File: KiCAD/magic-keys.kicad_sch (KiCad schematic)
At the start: 157 parts, among them J1 Keyswitch, K1 Keyswitch, M1 Keyswitch, P1 Keyswitch, Q1 Keyswitch, T1 Keyswitch, U1 Raspberry_Pi_Pico, U2 Keyswitch, X1 Keyswitch, Y1 Keyswitch

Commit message: added more stuff for magickeys
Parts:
- '"1, -_1, /1, 0)1, 1!1, 2@1, 3#1, 4$1, 5%1, 6^1, 7&1, 8*1, 9(1, ;:1, <,1, =+1, >.1, A1, B1, C1, D1, Down1, E1, F1, F10, F11, F12, F13, F2, F3, F4, F5, F6, F7, F8, F9, G1, H1, I1, J1, K1, L1, Left1, M1, N1, O1, P1, Q1, R1, Right1, S1, T1, U2, Up1, V1, W1, X1, Y1, Z1, [{1, ]}1, `~1: footprint ScottoKeebs_Choc:Choc_V1_1.00u -> ScottoKeebs_Hotswap:Hotswap_Choc_V1V2_1.00u
- Backspace1: footprint ScottoKeebs_Choc:Choc_V1_2.00u -> ScottoKeebs_Hotswap:Hotswap_Choc_V1V2_2.00u
- CapsLock1: footprint ScottoKeebs_Choc:Choc_V1_1.75u -> ScottoKeebs_Hotswap:Hotswap_Choc_V1V2_1.75u
- Cmd1, Cmd2, Control1, Fn1, Option1, Option2: footprint ScottoKeebs_Choc:Choc_V1_1.25u -> ScottoKeebs_Hotswap:Hotswap_Choc_V1V2_1.00u
- Del1, Esc1, \|1: footprint ScottoKeebs_Choc:Choc_V1_1.00u -> ScottoKeebs_Hotswap:Hotswap_Choc_V1V2_1.50u
- Enter1: footprint ScottoKeebs_Choc:Choc_V1_2.00u -> ScottoKeebs_Hotswap:Hotswap_Choc_V1V2_2.25u
- Shift1: footprint ScottoKeebs_Choc:Choc_V1_2.25u -> ScottoKeebs_Hotswap:Hotswap_Choc_V1V2_2.75u
- Shift2: footprint ScottoKeebs_Choc:Choc_V1_2.75u -> ScottoKeebs_Hotswap:Hotswap_Choc_V1V2_2.25u
- Space1: footprint ScottoKeebs_Choc:Choc_V1_6.25u -> ScottoKeebs_Hotswap:Hotswap_Choc_V1V2_5.50u
- Tab1: footprint ScottoKeebs_Choc:Choc_V1_1.50u -> ScottoKeebs_Hotswap:Hotswap_Choc_V1V2_1.50u

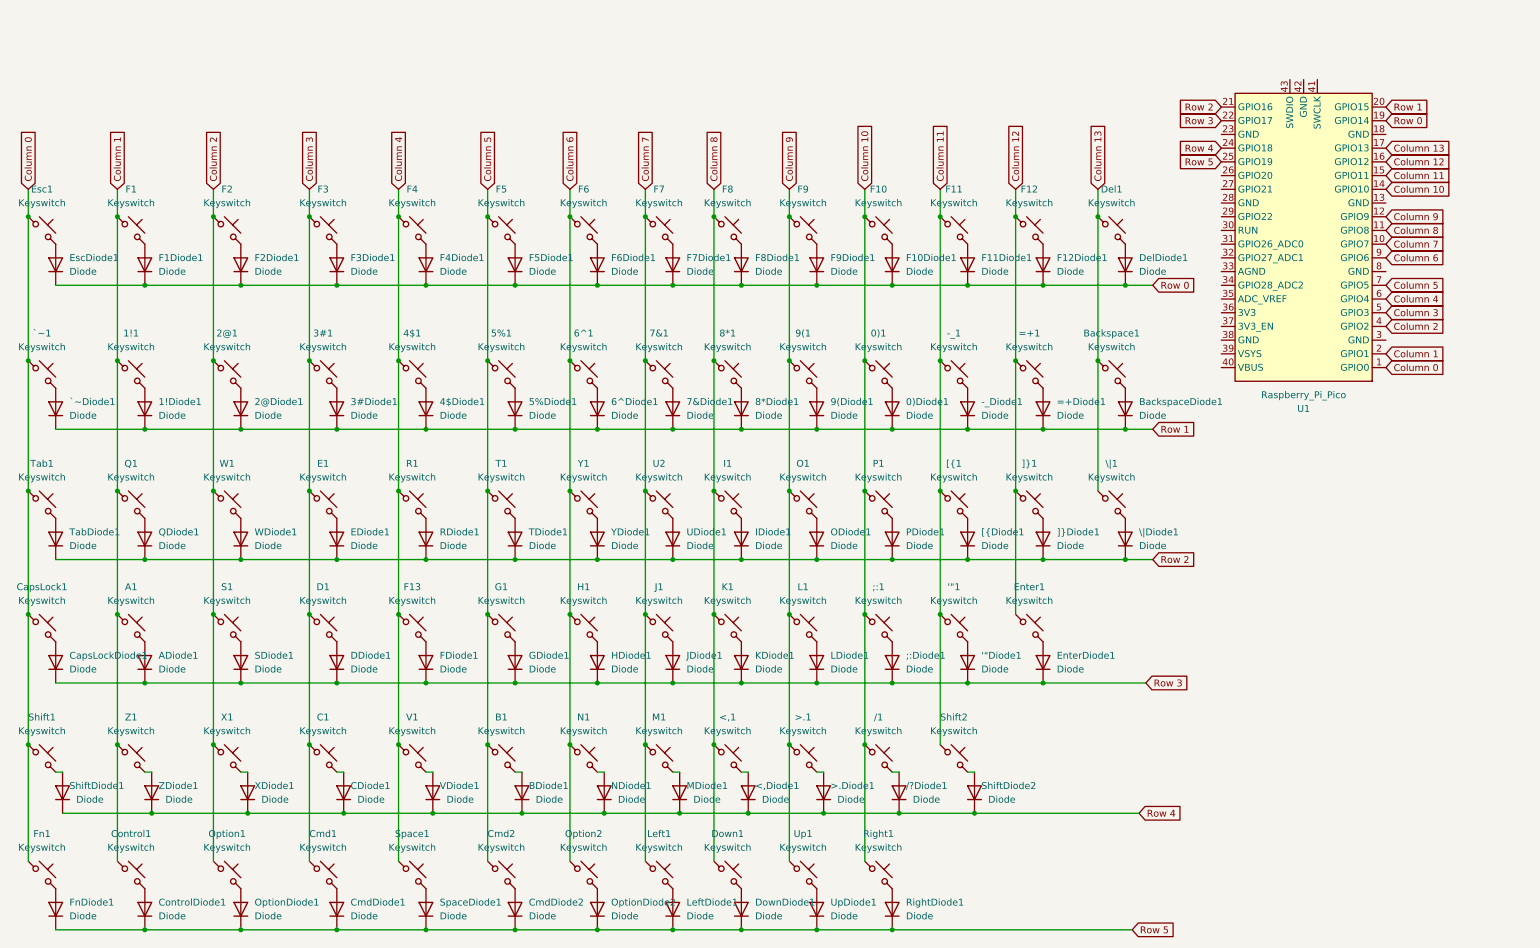
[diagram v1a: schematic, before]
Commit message: changed layout for stabs (to be keys), finished schematics
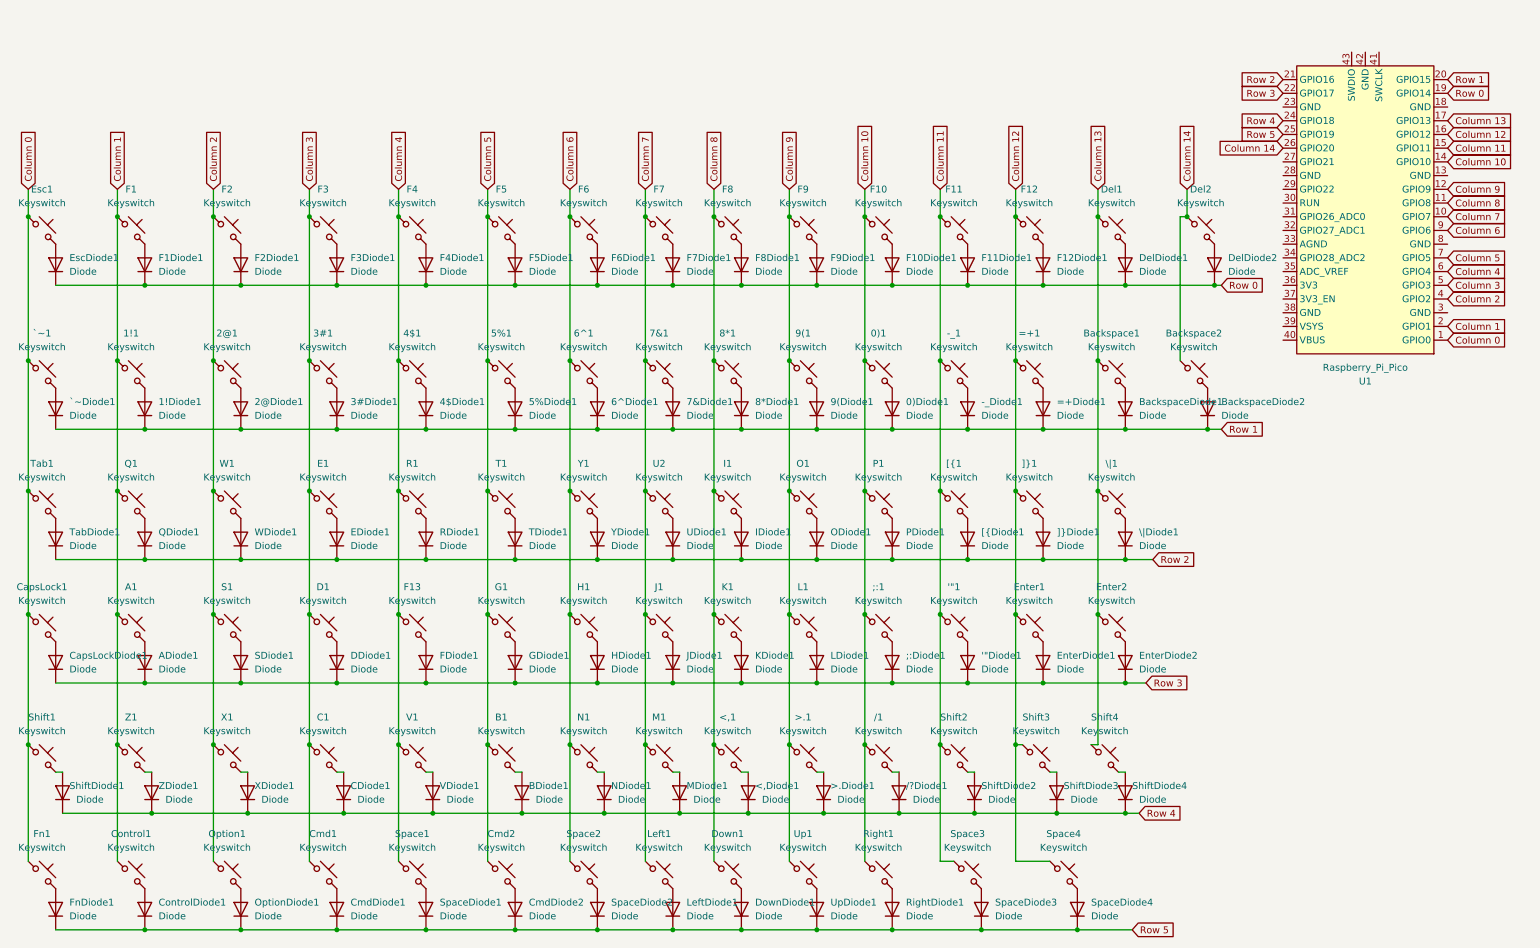
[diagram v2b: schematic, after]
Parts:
- removed Option2: Keyswitch, ScottoKeebs_Hotswap:Hotswap_Choc_V1V2_1.00u, symbol SCOTTO_KICAD_SYMBOLS:Placeholder_Keyswitch
- removed OptionDiode2: Diode, ScottoKeebs_Components:Diode_DO-35, symbol SCOTTO_KICAD_SYMBOLS:Placeholder_Diode
- added Backspace2, Del2, Shift4: Keyswitch, ScottoKeebs_Hotswap:Hotswap_Choc_V1_1.00u, symbol SCOTTO_KICAD_SYMBOLS:Placeholder_Keyswitch
- added BackspaceDiode2, DelDiode2, EnterDiode2, ShiftDiode3, ShiftDiode4, SpaceDiode2, SpaceDiode3, SpaceDiode4: Diode, ScottoKeebs_Components:Diode_DO-35, symbol SCOTTO_KICAD_SYMBOLS:Placeholder_Diode
- added Enter2: Keyswitch, ScottoKeebs_Hotswap:Hotswap_Choc_V1_1.25u, symbol SCOTTO_KICAD_SYMBOLS:Placeholder_Keyswitch
- added Shift3, Space2, Space3, Space4: Keyswitch, ScottoKeebs_Hotswap:Hotswap_Choc_V1_1.50u, symbol SCOTTO_KICAD_SYMBOLS:Placeholder_Keyswitch
- '"1, -_1, /1, 0)1, 1!1, 2@1, 3#1, 4$1, 5%1, 6^1, 7&1, 8*1, 9(1, ;:1, <,1, =+1, >.1, A1, B1, C1, Cmd1, Cmd2, Control1, D1, Down1, E1, F1, F10, F11, F12, F13, F2, F3, F4, F5, F6, F7, F8, F9, Fn1, G1, H1, I1, J1, K1, L1, Left1, M1, N1, O1, Option1, P1, Q1, R1, Right1, S1, T1, U2, Up1, V1, W1, X1, Y1, Z1, [{1, ]}1, `~1: footprint ScottoKeebs_Hotswap:Hotswap_Choc_V1V2_1.00u -> ScottoKeebs_Hotswap:Hotswap_Choc_V1_1.00u
- Backspace1: footprint ScottoKeebs_Hotswap:Hotswap_Choc_V1V2_2.00u -> ScottoKeebs_Hotswap:Hotswap_Choc_V1_1.00u
- CapsLock1: footprint ScottoKeebs_Hotswap:Hotswap_Choc_V1V2_1.75u -> ScottoKeebs_Hotswap:Hotswap_Choc_V1_1.75u
- Del1, Esc1: footprint ScottoKeebs_Hotswap:Hotswap_Choc_V1V2_1.50u -> ScottoKeebs_Hotswap:Hotswap_Choc_V1_1.00u
- Enter1: footprint ScottoKeebs_Hotswap:Hotswap_Choc_V1V2_2.25u -> ScottoKeebs_Hotswap:Hotswap_Choc_V1_1.00u
- Shift1: footprint ScottoKeebs_Hotswap:Hotswap_Choc_V1V2_2.75u -> ScottoKeebs_Hotswap:Hotswap_Choc_V1_1.25u
- Shift2: footprint ScottoKeebs_Hotswap:Hotswap_Choc_V1V2_2.25u -> ScottoKeebs_Hotswap:Hotswap_Choc_V1_1.25u
- Space1: footprint ScottoKeebs_Hotswap:Hotswap_Choc_V1V2_5.50u -> ScottoKeebs_Hotswap:Hotswap_Choc_V1_1.50u
- Tab1, \|1: footprint ScottoKeebs_Hotswap:Hotswap_Choc_V1V2_1.50u -> ScottoKeebs_Hotswap:Hotswap_Choc_V1_1.50u
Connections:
- net Column 11: now also Space3.1
- net Column 12: now also Shift3.1, Space4.1
- net Column 13: now also Enter2.1, Shift4.1
- net Column 6: now also Space2.1
- net Row 0: now also DelDiode2.1 (K)
- net Row 1: now also BackspaceDiode2.1 (K)
- net Row 3: now also EnterDiode2.1 (K)
- net Row 4: now also ShiftDiode3.1 (K), ShiftDiode4.1 (K)
- net Row 5: now also SpaceDiode2.1 (K), SpaceDiode3.1 (K), SpaceDiode4.1 (K)
- net Column 14: now reaches U1.26 (GPIO20)
- net Column 14: now also Backspace2.1, Del2.1
- new net: Backspace2.2, BackspaceDiode2.2 (A)
- new net: Shift4.2, ShiftDiode4.2 (A)
- new net: Shift3.2, ShiftDiode3.2 (A)
- new net: Space4.2, SpaceDiode4.2 (A)
- new net: Enter2.2, EnterDiode2.2 (A)
- new net: Space2.2, SpaceDiode2.2 (A)
- new net: Del2.2, DelDiode2.2 (A)
- new net: Space3.2, SpaceDiode3.2 (A)
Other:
- moved on the sheet: U1

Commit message: Optimised wiring
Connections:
- net Column 1: now also Shift3.1; no longer Z1.1
- net Column 10: now also >.1.1, Down1.1; no longer /1.1, Right1.1
- net Column 11: now also /1.1, Up1.1; no longer Shift2.1, Space3.1
- net Column 12: now also Right1.1, Shift2.1; no longer Shift3.1, Space4.1
- net Column 14: now also U1.19 (GPIO14); no longer U1.26 (GPIO20)
- net Column 2: now also Z1.1; no longer X1.1
- net Column 3: now also X1.1; no longer C1.1
- net Column 4: now also C1.1; no longer V1.1
- net Column 5: now also Space2.1, V1.1; no longer B1.1, Cmd2.1
- net Column 6: now also B1.1, Space3.1; no longer N1.1, Space2.1
- net Column 7: now also N1.1, Space4.1; no longer Left1.1, M1.1
- net Column 8: now also Cmd2.1, M1.1; no longer <,1.1, Down1.1
- net Column 9: now also <,1.1, Left1.1; no longer >.1.1, Up1.1
- net Row 0: now also U1.21 (GPIO16); no longer U1.19 (GPIO14)
- net Row 1: now also U1.22 (GPIO17); no longer U1.20 (GPIO15)
- net Row 2: now also U1.24 (GPIO18); no longer U1.21 (GPIO16)
- net Row 3: now also U1.25 (GPIO19); no longer U1.22 (GPIO17)
- net Row 4: now also U1.26 (GPIO20); no longer U1.24 (GPIO18)
- net Row 5: now also U1.27 (GPIO21); no longer U1.25 (GPIO19)
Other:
- moved on the sheet: /1, /?Diode1, <,1, <,Diode1, >.1, >.Diode1, B1, BDiode1, C1, CDiode1, Cmd2, Down1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

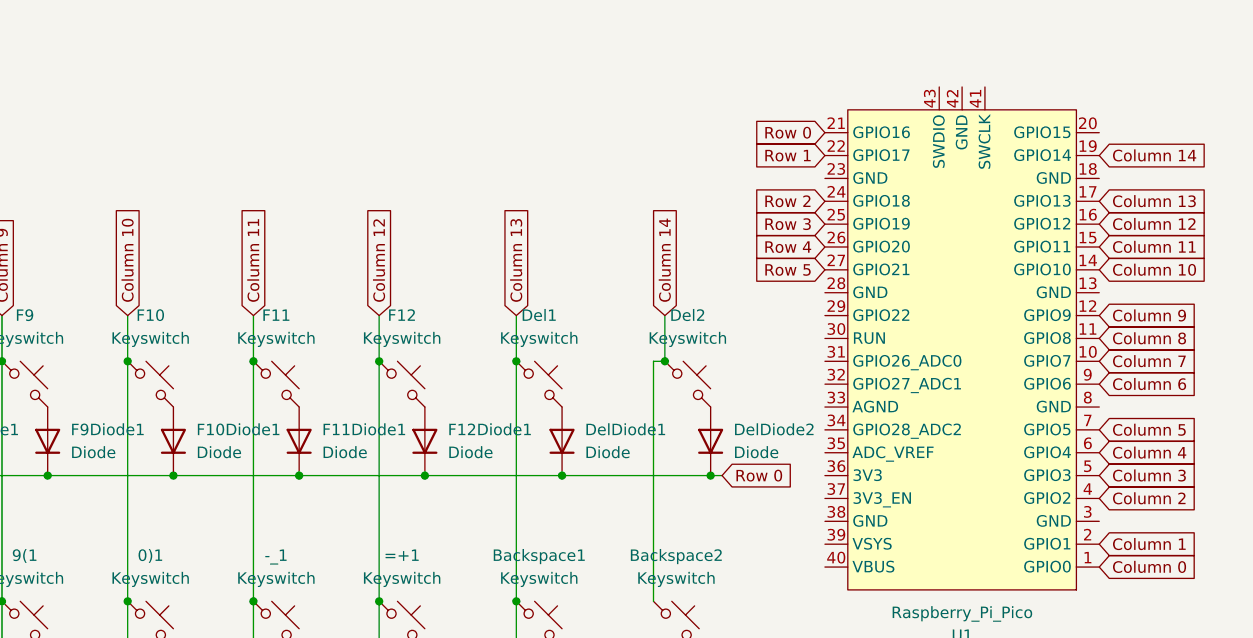
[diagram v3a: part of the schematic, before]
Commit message: added OLED screengit status
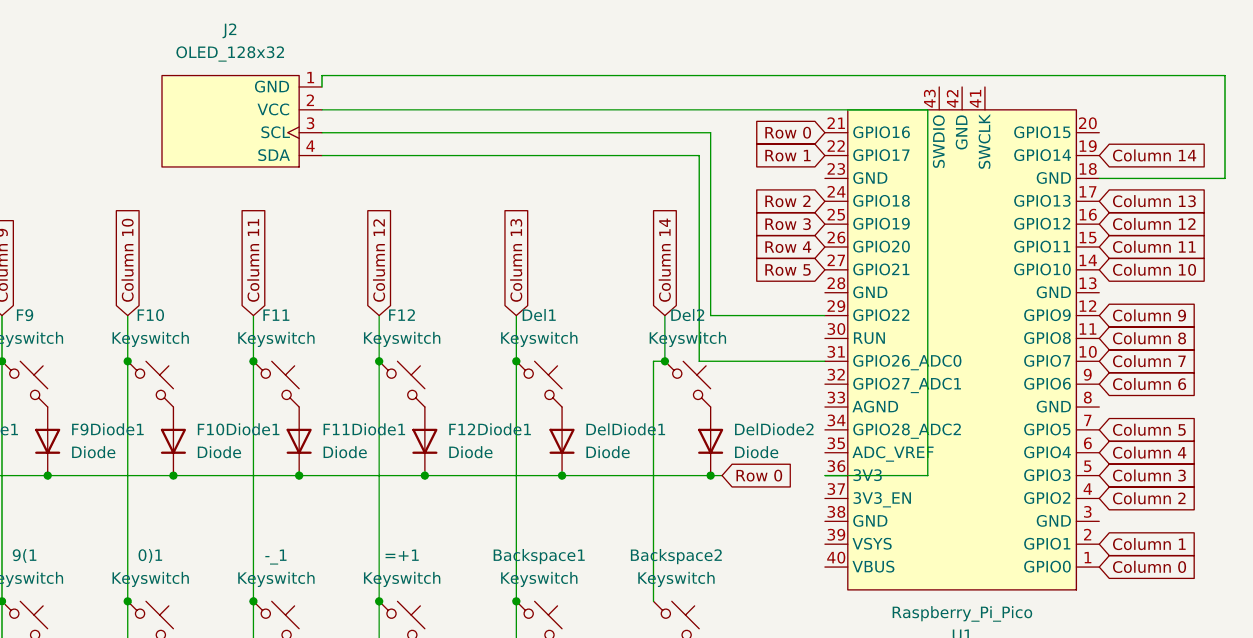
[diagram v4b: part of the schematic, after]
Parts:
- added J2: OLED_128x32, ScottoKeebs_Components:OLED_128x32, symbol SCOTTO_KICAD_SYMBOLS:OLED_128x32
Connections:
- net at U1.18 (GND): now also J2.1 (GND)
- net at U1.29 (GPIO22): now also J2.3 (SCL)
- net at U1.31 (GPIO26_ADC0): now also J2.4 (SDA)
- net at U1.36 (3V3): now also J2.2 (VCC)
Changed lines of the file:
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@@
 	(wire
 		(pts
+			(xy 294.64 8.89) (xy 194.31 8.89)
+		)
+		(stroke
+			(width 0)
+			(type default)
+		)
+	)
+	(wire
+		(pts
 			(xy 232.41 35.56) (xy 232.41 40.64)
 		)
@@
 	(wire
 		(pts
+			(xy 236.22 40.64) (xy 250.19 40.64)
+		)
+		(stroke
+			(width 0)
+			(type default)
+		)
+	)
+	(wire
+		(pts
 			(xy 83.82 114.3) (xy 86.36 114.3)
 		)
@@
 	(wire
 		(pts
+			(xy 280.67 20.32) (xy 294.64 20.32)
+		)
+		(stroke
+			(width 0)
+			(type default)
+		)
+	)
+	(wire
+		(pts
 			(xy 132.08 114.3) (xy 132.08 138.43)
 		)
@@
 	(wire
 		(pts
+			(xy 261.62 53.34) (xy 261.62 12.7)
+		)
+		(stroke
+			(width 0)
+			(type default)
+		)
+	)
+	(wire
+		(pts
 			(xy 236.22 80.01) (xy 220.98 80.01)
 		)
@@
 	(wire
 		(pts
+			(xy 250.19 53.34) (xy 261.62 53.34)
+		)
+		(stroke
+			(width 0)
+			(type default)
+		)
+	)
+	(wire
+		(pts
 			(xy 132.08 138.43) (xy 132.08 160.02)
 		)
@@
 	(wire
 		(pts
+			(xy 194.31 17.78) (xy 236.22 17.78)
+		)
+		(stroke
+			(width 0)
+			(type default)
+		)
+	)
+	(wire
+		(pts
 			(xy 17.78 40.64) (xy 17.78 67.31)
 		)
@@
 	(wire
 		(pts
+			(xy 294.64 20.32) (xy 294.64 8.89)
+		)
+		(stroke
+			(width 0)
+			(type default)
+		)
+	)
+	(wire
+		(pts
 			(xy 151.13 172.72) (xy 163.83 172.72)
 		)
@@
 	(wire
 		(pts
+			(xy 237.49 15.24) (xy 194.31 15.24)
+		)
+		(stroke
+			(width 0)
+			(type default)
+		)
+	)
+	(wire
+		(pts
 			(xy 48.26 138.43) (xy 48.26 160.02)
 		)
@@
 	(wire
 		(pts
+			(xy 194.31 8.89) (xy 194.31 10.16)
+		)
+		(stroke
+			(width 0)
+			(type default)
+		)
+	)
+	(wire
+		(pts
 			(xy 53.34 143.51) (xy 54.61 143.51)
 		)
@@
 	(wire
 		(pts
+			(xy 237.49 35.56) (xy 237.49 15.24)
+		)
+		(stroke
+			(width 0)
+			(type default)
+		)
+	)
+	(wire
+		(pts
 			(xy 231.14 67.31) (xy 231.14 40.64)
 		)
@@
 	(wire
 		(pts
+			(xy 261.62 12.7) (xy 194.31 12.7)
+		)
+		(stroke
+			(width 0)
+			(type default)
+		)
+	)
+	(wire
+		(pts
 			(xy 116.84 160.02) (xy 116.84 138.43)
 		)
@@
 	(wire
 		(pts
+			(xy 250.19 35.56) (xy 237.49 35.56)
+		)
+		(stroke
+			(width 0)
+			(type default)
+		)
+	)
+	(wire
+		(pts
 			(xy 172.72 114.3) (xy 172.72 138.43)
 		)
@@
 	(wire
 		(pts
+			(xy 236.22 17.78) (xy 236.22 40.64)
+		)
+		(stroke
+			(width 0)
+			(type default)
+		)
+	)
+	(wire
+		(pts
 			(xy 186.69 114.3) (xy 186.69 138.43)
 		)
@@
 					(unit 1)
 				)
+			)
+		)
+	)
+	(symbol
+		(lib_id "SCOTTO_KICAD_SYMBOLS:OLED_128x32")
+		(at 191.77 13.97 180)
+		(unit 1)
+		(exclude_from_sim no)
+		(in_bom yes)
+		(on_board yes)
+		(dnp no)
+		(fields_autoplaced yes)
+		(property "Reference" "J2"
+			(at 184.15 3.81 0)
+			(effects
+				(font
+					(size 1.27 1.27)
+				)
+			)
+		)
+		(property "Value" "OLED_128x32"
+			(at 184.15 6.35 0)
+			(effects
+				(font
+					(size 1.27 1.27)
+				)
+			)
+		)
+		(property "Footprint" "ScottoKeebs_Components:OLED_128x32"
+			(at 191.77 22.86 0)
+			(effects
+				(font
+					(size 1.27 1.27)
+				)
+				(hide yes)
+			)
+		)
+		(property "Datasheet" ""
+			(at 191.77 15.24 0)
+			(effects
+				(font
+					(size 1.27 1.27)
+				)
+				(hide yes)
+			)
+		)
+		(property "Description" ""
+			(at 191.77 13.97 0)
+			(effects
+				(font
+					(size 1.27 1.27)
+				)
+				(hide yes)
+			)
+		)
+		(pin "1"
+		)
+		(pin "3"
+		)
+		(pin "2"
+		)
+		(pin "4"
+		)
+		(instances
+			(project ""
+				(path "/6c6c6ef3-4ca2-4d45-83bf-72ee7546b384"
+					(reference "J2")
+					(unit 1)
+				)

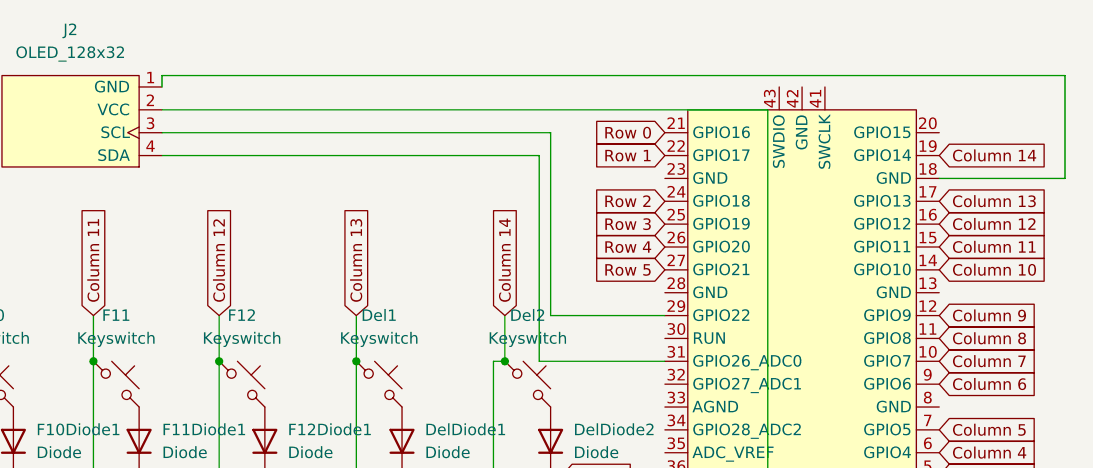
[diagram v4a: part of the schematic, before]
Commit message: updated BOM, retraced PCB for a nicer thing
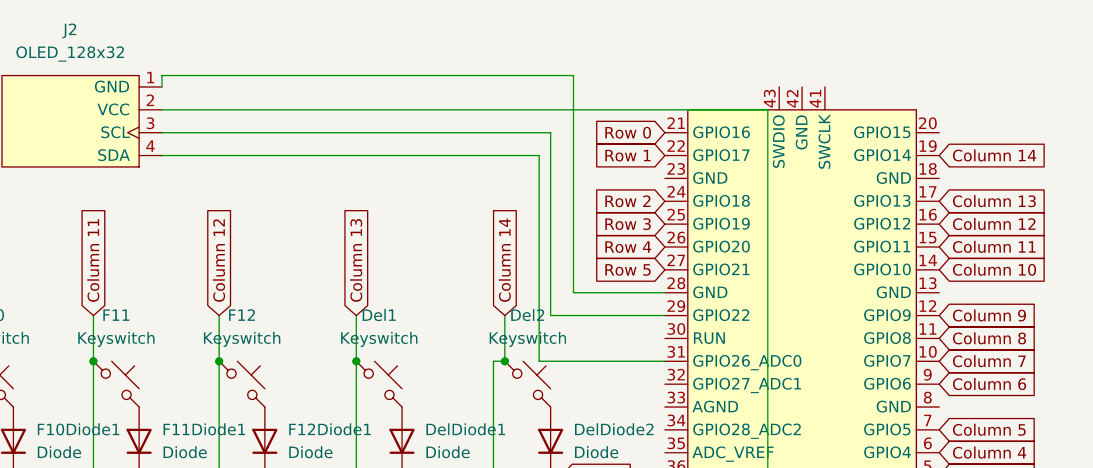
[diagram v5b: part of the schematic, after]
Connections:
- net at U1.18 (GND): no longer J2.1 (GND)
- net at U1.28 (GND): now also J2.1 (GND)
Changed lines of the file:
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@@
 (kicad_sch
-	(version 20231120)
+	(version 20250114)
 	(generator "eeschema")
-	(generator_version "8.0")
+	(generator_version "9.0")
 	(paper "A4")
 	(junction
@@
 	(wire
 		(pts
-			(xy 294.64 8.89) (xy 194.31 8.89)
-		)
-		(stroke
-			(width 0)
-			(type default)
-		)
-	)
-	(wire
-		(pts
 			(xy 232.41 35.56) (xy 232.41 40.64)
 		)
@@
 	(wire
 		(pts
-			(xy 280.67 20.32) (xy 294.64 20.32)
-		)
-		(stroke
-			(width 0)
-			(type default)
-		)
-	)
-	(wire
-		(pts
 			(xy 132.08 114.3) (xy 132.08 138.43)
 		)
@@
 	(wire
 		(pts
+			(xy 194.31 8.89) (xy 240.03 8.89)
+		)
+		(stroke
+			(width 0)
+			(type default)
+		)
+	)
+	(wire
+		(pts
 			(xy 123.19 80.01) (xy 137.16 80.01)
 		)
@@
 	(wire
 		(pts
-			(xy 294.64 20.32) (xy 294.64 8.89)
-		)
-		(stroke
-			(width 0)
-			(type default)
-		)
-	)
-	(wire
-		(pts
 			(xy 151.13 172.72) (xy 163.83 172.72)
 		)
@@
 	(wire
 		(pts
+			(xy 240.03 8.89) (xy 240.03 33.02)
+		)
+		(stroke
+			(width 0)
+			(type default)
+		)
+	)
+	(wire
+		(pts
 			(xy 34.29 40.64) (xy 34.29 67.31)
 		)
@@
 	(wire
 		(pts
+			(xy 240.03 33.02) (xy 250.19 33.02)
+		)
+		(stroke
+			(width 0)
+			(type default)
+		)
+	)
+	(wire
+		(pts
 			(xy 39.37 80.01) (xy 57.15 80.01)
 		)
@@
 		)
 	)
+	(embedded_fonts no)
 )
